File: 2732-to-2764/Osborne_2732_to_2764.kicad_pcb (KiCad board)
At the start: 2 copper layers, 21.6 x 41.7 mm, 4 parts, among them J1 2732, J2 2764, J3 A12

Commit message: Corrected Gerbers for PCBWAY (still pending testing)
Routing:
- net GND: track 40.9 -> 0.00 mm
- net VCC: track 29.0 -> 25.7 mm
- added copper zone on F.Cu, net GND
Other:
- board size 21.6 x 41.7 mm -> 22.4 x 42.4 mm
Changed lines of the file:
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@@
     )
   )
-  (gr_rect (start 144.272 56.388) (end 165.862 98.044)
-    (stroke (width 0.1) (type default)) (fill none) (layer "Edge.Cuts"))
+  (gr_line (start 144.318431 56.066371) (end 165.670431 56.066371)
+    (stroke (width 0.1) (type default)) (layer "Edge.Cuts"))
+  (gr_line (start 166.170431 56.566371) (end 166.170431 97.984371)
+    (stroke (width 0.1) (type default)) (layer "Edge.Cuts"))
+  (gr_line (start 143.818431 97.984371) (end 143.818431 56.566371)
+    (stroke (width 0.1) (type default)) (layer "Edge.Cuts"))
+  (gr_arc (start 143.818431 56.566371) (mid 143.964878 56.212818) (end 144.318431 56.066371)
+    (stroke (width 0.1) (type default)) (layer "Edge.Cuts"))
+  (gr_line (start 165.670431 98.484371) (end 144.318431 98.484371)
+    (stroke (width 0.1) (type default)) (layer "Edge.Cuts"))
+  (gr_arc (start 165.670431 56.066371) (mid 166.023975 56.212827) (end 166.170431 56.566371)
+    (stroke (width 0.1) (type default)) (layer "Edge.Cuts"))
+  (gr_arc (start 144.318431 98.484371) (mid 143.964868 98.337934) (end 143.818431 97.984371)
+    (stroke (width 0.1) (type default)) (layer "Edge.Cuts"))
+  (gr_arc (start 166.170431 97.984371) (mid 166.023997 98.337954) (end 165.670431 98.484371)
+    (stroke (width 0.1) (type default)) (layer "Edge.Cuts"))
   (gr_text "2732-to-2764 Converter\nBrett Hallen\nAug 2024" (at 156.718 74.168 90) (layer "B.SilkS")
     (effects (font (size 1 1) (thickness 0.1875)) (justify left bottom mirror))
   )
-  (segment (start 145.796 68.072) (end 148.59 68.072) (width 0.25) (layer "B.Cu") (net 1))
-  (segment (start 145.796 70.612) (end 148.59 70.612) (width 0.25) (layer "B.Cu") (net 2))
-  (segment (start 145.796 73.152) (end 148.59 73.152) (width 0.25) (layer "B.Cu") (net 3))
-  (segment (start 145.796 75.692) (end 148.59 75.692) (width 0.25) (layer "B.Cu") (net 4))
-  (segment (start 145.796 78.232) (end 148.59 78.232) (width 0.25) (layer "B.Cu") (net 5))
-  (segment (start 145.796 80.772) (end 148.59 80.772) (width 0.25) (layer "B.Cu") (net 6))
-  (segment (start 145.796 83.312) (end 148.59 83.312) (width 0.25) (layer "B.Cu") (net 7))
-  (segment (start 145.796 85.852) (end 148.59 85.852) (width 0.25) (layer "B.Cu") (net 8))
-  (segment (start 145.796 88.392) (end 148.59 88.392) (width 0.25) (layer "B.Cu") (net 9))
-  (segment (start 145.796 90.932) (end 148.59 90.932) (width 0.25) (layer "B.Cu") (net 10))
-  (segment (start 145.796 93.472) (end 148.59 93.472) (width 0.25) (layer "B.Cu") (net 11))
-  (segment (start 148.8718 94.8851) (end 149.7169 94.04) (width 0.25) (layer "F.Cu") (net 12))
-  (segment (start 148.59 96.012) (end 148.59 94.8851) (width 0.25) (layer "F.Cu") (net 12))
-  (segment (start 148.59 94.8851) (end 148.8718 94.8851) (width 0.25) (layer "F.Cu") (net 12))
-  (segment (start 149.7169 94.04) (end 149.7169 60.9828) (width 0.25) (layer "F.Cu") (net 12))
-  (segment (start 148.839 58.928) (end 148.839 60.1049) (width 0.25) (layer "F.Cu") (net 12))
-  (segment (start 149.7169 60.9828) (end 148.839 60.1049) (width 0.25) (layer "F.Cu") (net 12))
-  (segment (start 145.796 96.012) (end 148.59 96.012) (width 0.25) (layer "B.Cu") (net 12))
-  (segment (start 161.036 96.012) (end 163.83 96.012) (width 0.25) (layer "B.Cu") (net 13))
-  (segment (start 161.036 93.472) (end 163.83 93.472) (width 0.25) (layer "B.Cu") (net 14))
-  (segment (start 161.036 90.932) (end 163.83 90.932) (width 0.25) (layer "B.Cu") (net 15))
-  (segment (start 161.036 88.392) (end 163.83 88.392) (width 0.25) (layer "B.Cu") (net 16))
-  (segment (start 161.036 85.852) (end 163.83 85.852) (width 0.25) (layer "B.Cu") (net 17))
-  (segment (start 161.036 83.312) (end 163.83 83.312) (width 0.25) (layer "B.Cu") (net 18))
-  (segment (start 161.036 80.772) (end 163.83 80.772) (width 0.25) (layer "B.Cu") (net 19))
-  (segment (start 161.036 78.232) (end 163.83 78.232) (width 0.25) (layer "B.Cu") (net 20))
-  (segment (start 161.036 75.692) (end 163.83 75.692) (width 0.25) (layer "B.Cu") (net 21))
-  (segment (start 161.036 73.152) (end 163.83 73.152) (width 0.25) (layer "B.Cu") (net 22))
-  (segment (start 161.036 70.612) (end 163.83 70.612) (width 0.25) (layer "B.Cu") (net 23))
-  (segment (start 163.801 58.928) (end 163.801 60.0549) (width 0.25) (layer "F.Cu") (net 24))
-  (segment (start 163.83 60.0839) (end 163.801 60.0549) (width 0.25) (layer "F.Cu") (net 24))
-  (segment (start 163.83 62.992) (end 163.83 60.0839) (width 0.25) (layer "F.Cu") (net 24))
-  (segment (start 163.83 65.532) (end 163.83 62.992) (width 0.25) (layer "F.Cu") (net 24))
-  (segment (start 163.576 66.6589) (end 163.83 66.6589) (width 0.25) (layer "B.Cu") (net 24))
-  (segment (start 161.036 68.072) (end 162.1629 68.072) (width 0.25) (layer "B.Cu") (net 24))
-  (segment (start 148.2591 66.802) (end 158.6391 66.802) (width 0.25) (layer "B.Cu") (net 24))
-  (segment (start 163.83 65.532) (end 163.83 66.6589) (width 0.25) (layer "B.Cu") (net 24))
-  (segment (start 147.4456 64.1364) (end 147.4456 65.9885) (width 0.25) (layer "B.Cu") (net 24))
-  (segment (start 158.6391 66.802) (end 159.9091 68.072) (width 0.25) (layer "B.Cu") (net 24))
-  (segment (start 161.036 68.072) (end 159.9091 68.072) (width 0.25) (layer "B.Cu") (net 24))
-  (segment (start 148.59 62.992) (end 147.4456 64.1364) (width 0.25) (layer "B.Cu") (net 24))
-  (segment (start 147.4456 65.9885) (end 148.2591 66.802) (width 0.25) (layer "B.Cu") (net 24))
-  (segment (start 162.1629 68.072) (end 163.576 66.6589) (width 0.25) (layer "B.Cu") (net 24))
+  (segment (start 148.59 68.072) (end 145.796 68.072) (width 0.25) (layer "B.Cu") (net 1))
+  (segment (start 148.59 70.612) (end 145.796 70.612) (width 0.25) (layer "B.Cu") (net 2))
+  (segment (start 148.59 73.152) (end 145.796 73.152) (width 0.25) (layer "B.Cu") (net 3))
+  (segment (start 148.59 75.692) (end 145.796 75.692) (width 0.25) (layer "B.Cu") (net 4))
+  (segment (start 148.59 78.232) (end 145.796 78.232) (width 0.25) (layer "B.Cu") (net 5))
+  (segment (start 148.59 80.772) (end 145.796 80.772) (width 0.25) (layer "B.Cu") (net 6))
+  (segment (start 148.59 83.312) (end 145.796 83.312) (width 0.25) (layer "B.Cu") (net 7))
+  (segment (start 148.59 85.852) (end 145.796 85.852) (width 0.25) (layer "B.Cu") (net 8))
+  (segment (start 148.59 88.392) (end 145.796 88.392) (width 0.25) (layer "B.Cu") (net 9))
+  (segment (start 148.59 90.932) (end 145.796 90.932) (width 0.25) (layer "B.Cu") (net 10))
+  (segment (start 148.59 93.472) (end 145.796 93.472) (width 0.25) (layer "B.Cu") (net 11))
+  (segment (start 163.83 96.012) (end 161.036 96.012) (width 0.25) (layer "B.Cu") (net 13))
+  (segment (start 163.83 93.472) (end 161.036 93.472) (width 0.25) (layer "B.Cu") (net 14))
+  (segment (start 163.83 90.932) (end 161.036 90.932) (width 0.25) (layer "B.Cu") (net 15))
+  (segment (start 163.83 88.392) (end 161.036 88.392) (width 0.25) (layer "B.Cu") (net 16))
+  (segment (start 163.83 85.852) (end 161.036 85.852) (width 0.25) (layer "B.Cu") (net 17))
+  (segment (start 163.83 83.312) (end 161.036 83.312) (width 0.25) (layer "B.Cu") (net 18))
+  (segment (start 163.83 80.772) (end 161.036 80.772) (width 0.25) (layer "B.Cu") (net 19))
+  (segment (start 163.83 78.232) (end 161.036 78.232) (width 0.25) (layer "B.Cu") (net 20))
+  (segment (start 163.83 75.692) (end 161.036 75.692) (width 0.25) (layer "B.Cu") (net 21))
+  (segment (start 163.83 73.152) (end 161.036 73.152) (width 0.25) (layer "B.Cu") (net 22))
+  (segment (start 163.83 70.612) (end 161.036 70.612) (width 0.25) (layer "B.Cu") (net 23))
+  (segment (start 163.83 62.992) (end 163.83 65.532) (width 0.25) (layer "F.Cu") (net 24))
+  (segment (start 154.8291 62.992) (end 159.9091 68.072) (width 0.25) (layer "F.Cu") (net 24))
+  (segment (start 163.83 62.992) (end 163.83 61.8651) (width 0.25) (layer "F.Cu") (net 24))
+  (segment (start 163.801 58.928) (end 163.801 61.8361) (width 0.25) (layer "F.Cu") (net 24))
+  (segment (start 161.036 68.072) (end 159.9091 68.072) (width 0.25) (layer "F.Cu") (net 24))
+  (segment (start 163.801 61.8361) (end 163.83 61.8651) (width 0.25) (layer "F.Cu") (net 24))
+  (segment (start 148.59 62.992) (end 154.8291 62.992) (width 0.25) (layer "F.Cu") (net 24))
+  (segment (start 163.83 65.532) (end 162.7031 65.532) (width 0.25) (layer "B.Cu") (net 24))
+  (segment (start 162.7031 65.532) (end 161.29 66.9451) (width 0.25) (layer "B.Cu") (net 24))
+  (segment (start 161.29 66.9451) (end 161.036 66.9451) (width 0.25) (layer "B.Cu") (net 24))
+  (segment (start 161.036 68.072) (end 161.036 66.9451) (width 0.25) (layer "B.Cu") (net 24))
+  (segment (start 148.59 65.532) (end 148.59 64.4051) (width 0.25) (layer "B.Cu") (net 25))
+  (segment (start 161.261 58.928) (end 151.379 58.928) (width 0.25) (layer "B.Cu") (net 25))
   (segment (start 151.379 62.3204) (end 151.379 58.928) (width 0.25) (layer "B.Cu") (net 25))
-  (segment (start 151.379 58.928) (end 161.261 58.928) (width 0.25) (layer "B.Cu") (net 25))
   (segment (start 148.59 64.4051) (end 149.2943 64.4051) (width 0.25) (layer "B.Cu") (net 25))
-  (segment (start 148.59 65.532) (end 148.59 64.4051) (width 0.25) (layer "B.Cu") (net 25))
   (segment (start 149.2943 64.4051) (end 151.379 62.3204) (width 0.25) (layer "B.Cu") (net 25))
-  (zone (net 0) (net_name "") (layer "Edge.Cuts") (hatch edge 0.5)
+  (zone (net 12) (net_name "GND") (layer "F.Cu") (hatch edge 0.5)
     (connect_pads (clearance 0.5))
     (min_thickness 0.25) (filled_areas_thickness no)
@@
     (polygon
       (pts
-        (xy 144.272 98.044)
-        (xy 144.272 56.388)
-        (xy 165.862 56.388)
-        (xy 165.862 98.044)
+        (xy 166.624 55.626)
+        (xy 166.624 98.806)
+        (xy 143.002 98.806)
+        (xy 143.002 55.626)
+        (xy 143.256 55.626)
       )
     )

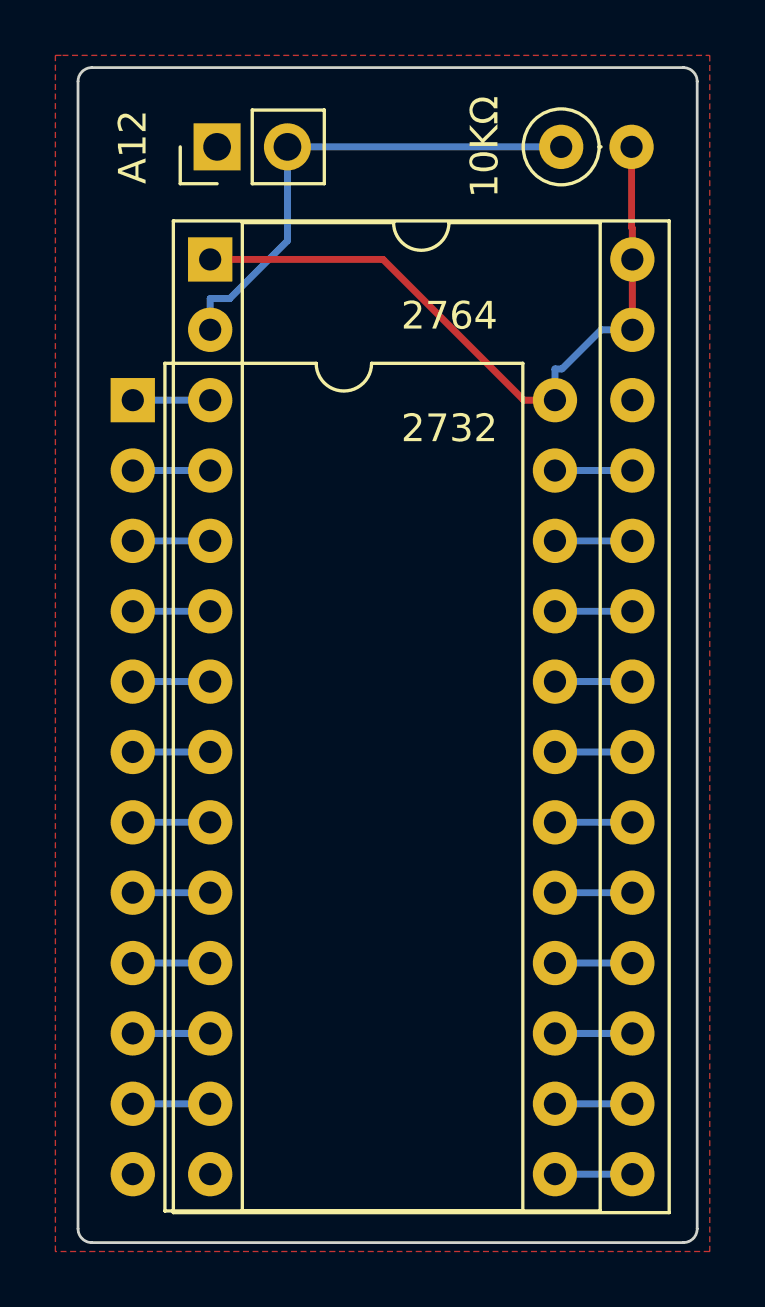
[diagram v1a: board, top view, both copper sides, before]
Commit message: Updated socket pins
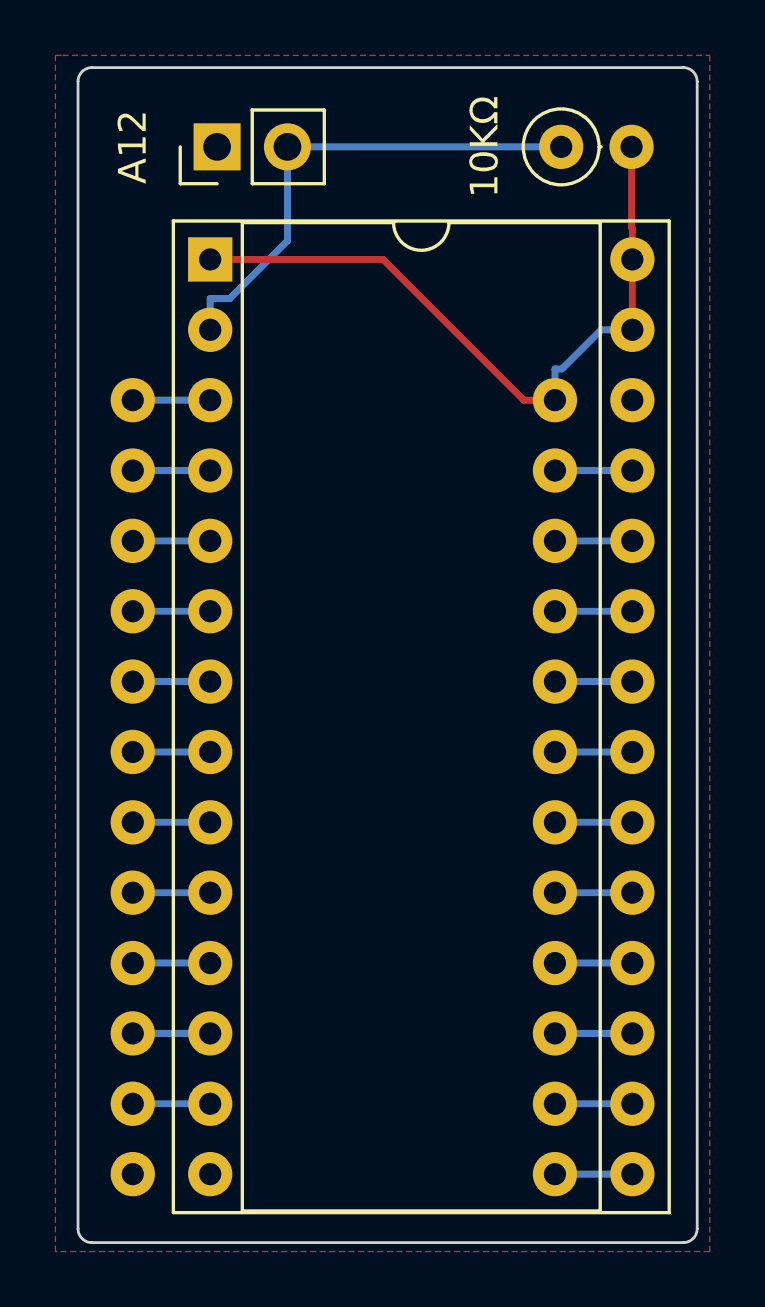
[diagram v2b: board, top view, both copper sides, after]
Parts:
- J1: value 2732 -> 2732_ROM_Socket; footprint Package_DIP:DIP-24_W15.24mm -> Open2327RomAdapter:DIP-24_W15.24mm-Notch
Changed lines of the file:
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@@
     )
   )
-  (footprint "Package_DIP:DIP-24_W15.24mm" (layer "F.Cu")
+  (footprint "Open2327RomAdapter:DIP-24_W15.24mm-Notch" (layer "F.Cu")
     (at 145.796 68.072)
-    (descr "24-lead though-hole mounted DIP package, row spacing 15.24 mm (600 mils)")
-    (tags "THT DIP DIL PDIP 2.54mm 15.24mm 600mil")
+    (descr "24-lead dip package, row spacing 15.24 mm (600 mils)")
+    (tags "dil dip 2.54 600")
     (property "Sheetfile" "Osborne_2732_to_2764.kicad_sch")
     (property "Sheetname" "")
@@
     (property "ki_keywords" "connector")
     (attr through_hole)
-    (fp_text reference "J1" (at 7.62 -2.33) (layer "F.SilkS") hide
+    (fp_text reference "J1" (at 7.62 5.08) (layer "F.SilkS") hide
         (effects (font (size 1 1) (thickness 0.15)))
     )
-    (fp_text value "2732" (at 11.43 1.016 180) (layer "F.SilkS")
+    (fp_text value "2732_ROM_Socket" (at 0 -3.72) (layer "F.Fab") hide
         (effects (font (size 1 1) (thickness 0.15)))
     )
-    (fp_text user "${REFERENCE}" (at 7.62 13.97) (layer "F.Fab") hide
-        (effects (font (size 1 1) (thickness 0.15)))
-    )
-    (fp_line (start 1.16 -1.33) (end 1.16 29.27)
-      (stroke (width 0.12) (type solid)) (layer "F.SilkS"))
-    (fp_line (start 1.16 29.27) (end 14.08 29.27)
-      (stroke (width 0.12) (type solid)) (layer "F.SilkS"))
-    (fp_line (start 6.62 -1.33) (end 1.16 -1.33)
-      (stroke (width 0.12) (type solid)) (layer "F.SilkS"))
-    (fp_line (start 14.08 -1.33) (end 8.62 -1.33)
-      (stroke (width 0.12) (type solid)) (layer "F.SilkS"))
-    (fp_line (start 14.08 29.27) (end 14.08 -1.33)
-      (stroke (width 0.12) (type solid)) (layer "F.SilkS"))
-    (fp_arc (start 8.62 -1.33) (mid 7.62 -0.33) (end 6.62 -1.33)
-      (stroke (width 0.12) (type solid)) (layer "F.SilkS"))
-    (fp_line (start -1.05 -1.55) (end -1.05 29.5)
+    (fp_line (start -0.889 -1.016) (end 0.889 -1.016)
+      (stroke (width 0.15) (type solid)) (layer "B.SilkS"))
+    (fp_line (start -0.889 28.956) (end -0.889 -1.016)
+      (stroke (width 0.15) (type solid)) (layer "B.SilkS"))
+    (fp_line (start 0.889 -1.016) (end 0.889 28.956)
+      (stroke (width 0.15) (type solid)) (layer "B.SilkS"))
+    (fp_line (start 0.889 28.956) (end -0.889 28.956)
+      (stroke (width 0.15) (type solid)) (layer "B.SilkS"))
+    (fp_line (start 14.351 -1.016) (end 16.129 -1.016)
+      (stroke (width 0.15) (type solid)) (layer "B.SilkS"))
+    (fp_line (start 14.351 28.956) (end 14.351 -1.016)
+      (stroke (width 0.15) (type solid)) (layer "B.SilkS"))
+    (fp_line (start 16.129 -1.016) (end 16.129 28.956)
+      (stroke (width 0.15) (type solid)) (layer "B.SilkS"))
+    (fp_line (start 16.129 28.956) (end 14.351 28.956)
+      (stroke (width 0.15) (type solid)) (layer "B.SilkS"))
+    (fp_line (start -1.05 -2.45) (end -1.05 30.4)
       (stroke (width 0.05) (type solid)) (layer "F.CrtYd"))
-    (fp_line (start -1.05 29.5) (end 16.3 29.5)
+    (fp_line (start -1.05 -2.45) (end 16.3 -2.45)
       (stroke (width 0.05) (type solid)) (layer "F.CrtYd"))
-    (fp_line (start 16.3 -1.55) (end -1.05 -1.55)
+    (fp_line (start -1.05 30.4) (end 16.3 30.4)
       (stroke (width 0.05) (type solid)) (layer "F.CrtYd"))
-    (fp_line (start 16.3 29.5) (end 16.3 -1.55)
+    (fp_line (start 16.3 -2.45) (end 16.3 30.4)
       (stroke (width 0.05) (type solid)) (layer "F.CrtYd"))
-    (fp_line (start 0.255 -0.27) (end 1.255 -1.27)
-      (stroke (width 0.1) (type solid)) (layer "F.Fab"))
-    (fp_line (start 0.255 29.21) (end 0.255 -0.27)
-      (stroke (width 0.1) (type solid)) (layer "F.Fab"))
-    (fp_line (start 1.255 -1.27) (end 14.985 -1.27)
-      (stroke (width 0.1) (type solid)) (layer "F.Fab"))
-    (fp_line (start 14.985 -1.27) (end 14.985 29.21)
-      (stroke (width 0.1) (type solid)) (layer "F.Fab"))
-    (fp_line (start 14.985 29.21) (end 0.255 29.21)
-      (stroke (width 0.1) (type solid)) (layer "F.Fab"))
-    (pad "1" thru_hole rect (at 0 0) (size 1.6 1.6) (drill 0.8) (layers "*.Cu" "*.Mask")
+    (pad "1" thru_hole oval (at 0 0) (size 1.6 1.6) (drill 0.8) (layers "*.Cu" "*.Mask")
       (net 1 "A07") (pinfunction "Pin_1") (pintype "passive"))
     (pad "2" thru_hole oval (at 0 2.54) (size 1.6 1.6) (drill 0.8) (layers "*.Cu" "*.Mask")
@@
     (pad "24" thru_hole oval (at 15.24 0) (size 1.6 1.6) (drill 0.8) (layers "*.Cu" "*.Mask")
       (net 24 "VCC") (pinfunction "Pin_24") (pintype "passive"))
-    (model "${KICAD6_3DMODEL_DIR}/Package_DIP.3dshapes/DIP-24_W15.24mm.wrl"
-      (offset (xyz 0 0 0))
+    (model "${KISYS3DMOD}/Connector_PinHeader_2.54mm.3dshapes/PinHeader_1x12_P2.54mm_Vertical.step"
+      (offset (xyz 0 0 -2))
       (scale (xyz 1 1 1))
-      (rotate (xyz 0 0 0))
+      (rotate (xyz 0 180 0))
+    )
+    (model "${KISYS3DMOD}/Connector_PinHeader_2.54mm.3dshapes/PinHeader_1x12_P2.54mm_Vertical.step"
+      (offset (xyz 15.24 0 -2))
+      (scale (xyz 1 1 1))
+      (rotate (xyz 0 -180 0))
     )
   )
@@
         (effects (font (size 1 1) (thickness 0.15)))
     )
-    (fp_text value "2764" (at 8.636 2.032) (layer "F.SilkS")
+    (fp_text value "2764" (at 8.636 2.032) (layer "F.SilkS") hide
         (effects (font (size 1 1) (thickness 0.15)))
     )
